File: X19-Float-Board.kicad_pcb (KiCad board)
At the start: 2 copper layers, 0 parts

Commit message: started layout
in meeting
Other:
- board outline added: 100 x 100 mm
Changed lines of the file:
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@@
 		)
+	)
+	(gr_circle
+		(center 150 100)
+		(end 200 100)
+		(stroke
+			(width 0.05)
+			(type solid)
+		)
+		(fill no)
+		(layer "Edge.Cuts")
 	)
 	(embedded_fonts no)

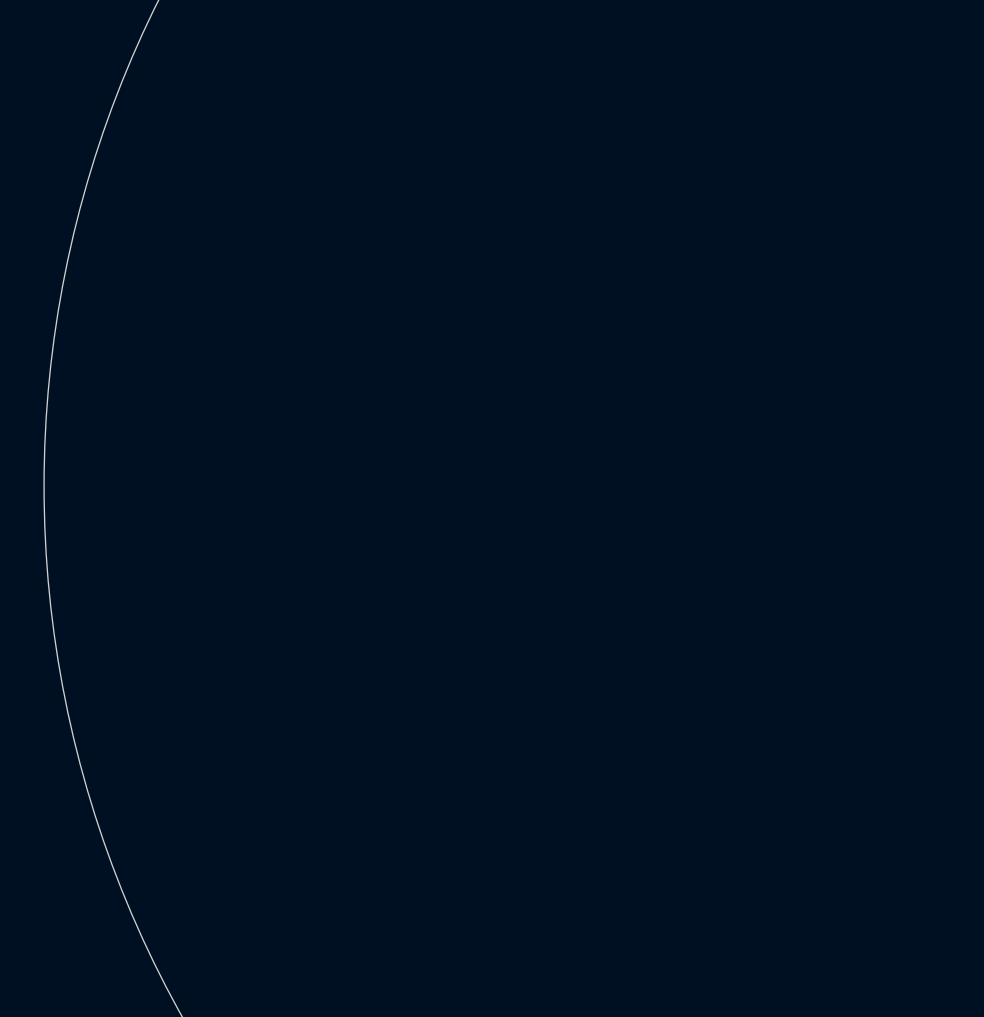
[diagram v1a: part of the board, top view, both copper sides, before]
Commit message: Footprint
Found footprints for multiple components and imported them to be used in PCB
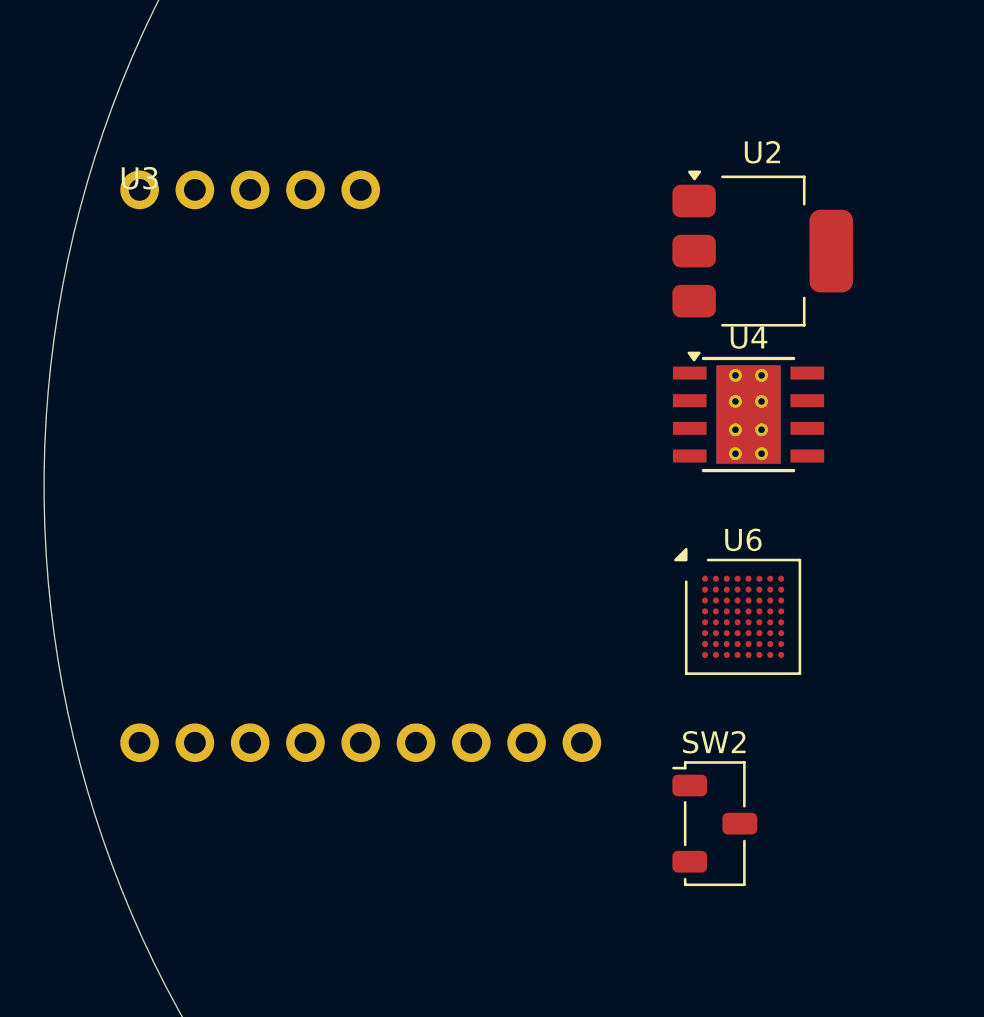
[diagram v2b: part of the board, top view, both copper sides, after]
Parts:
- added SW2: SW_Nidec_CAS-120A1, Button_Switch_SMD:Nidec_Copal_CAS-120A, F.Cu at (130.8, 115.5)
- added U2: AMS1117-3.3, Package_TO_SOT_SMD:SOT-223-3_TabPin2, F.Cu at (133.0, 89.2)
- added U3: RFM95W-868S2, customrf:rf module, F.Cu at (104.4, 86.4)
- added U4: TPS54336ADDA, Package_SO:TI_SO-PowerPAD-8_ThermalVias, F.Cu at (132.4, 96.7)
- added U6: STM32G431RBIx, Package_BGA:UFBGA-64_5x5mm_Layout8x8_P0.5mm, F.Cu at (132.1, 106.0)

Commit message: Custom RF module and component
Created my own setup for the footprint for the custom RF module
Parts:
- removed U3: RFM95W-868S2, customrf:rf module
- added C1: 100nF, Capacitor_SMD:C_0603_1608Metric, F.Cu at (169.6, 93.3)
- added C10: 100nF, Capacitor_SMD:C_0603_1608Metric, F.Cu at (162.0, 113.1)
- added C11: 100nF, Capacitor_SMD:C_0603_1608Metric, F.Cu at (163.6, 93.3)
- added C12: 100nF, Capacitor_SMD:C_0603_1608Metric, F.Cu at (169.6, 122.3)
- added C13: 100nF, Capacitor_SMD:C_0603_1608Metric, F.Cu at (175.6, 119.8)
- added C14: 4.7µF, Capacitor_SMD:C_0603_1608Metric, F.Cu at (169.6, 112.8)
- added C15: 4.7µF, Capacitor_SMD:C_0603_1608Metric, F.Cu at (169.6, 115.3)
- added C16: 4.7µF, Capacitor_SMD:C_0603_1608Metric, F.Cu at (169.6, 117.8)
- added C2: 27nF, Capacitor_SMD:C_0603_1608Metric, F.Cu at (169.6, 95.8)
- added C3: 10µF, Capacitor_SMD:C_0603_1608Metric, F.Cu at (169.6, 98.3)
- added C4: 120pF, Capacitor_SMD:C_0603_1608Metric, F.Cu at (169.6, 100.8)
- added C5: .012µF, Capacitor_SMD:C_0603_1608Metric, F.Cu at (169.6, 103.3)
- added C6: 0.1µF, Capacitor_SMD:C_0603_1608Metric, F.Cu at (173.6, 93.3)
- added C7: 47µF, Capacitor_SMD:C_0603_1608Metric, F.Cu at (173.6, 95.8)
- added C8: 47µF, Capacitor_SMD:C_0603_1608Metric, F.Cu at (173.6, 98.3)
- added C9: 100nF, Capacitor_SMD:C_0603_1608Metric, F.Cu at (175.6, 112.8)
- added D1: D_Schottky, Diode_SMD:D_SOD-123, F.Cu at (160.9, 105.0)
- added F1: 2A 12V PTC fuse, Fuse:Fuse_1812_4532Metric, F.Cu at (171.0, 107.0)
- added J1: Motor, TerminalBlock_Altech:Altech_AK100_1x02_P5.00mm, F.Cu at (153.0, 98.0)
- added J2: Conn_01x04_Pin, Connector_JST:JST_GH_BM04B-GHS-TBT_1x04-1MP_P1.25mm_Vertical, F.Cu at (154.8, 115.7)
- added L1: 15µH, Capacitor_SMD:C_0603_1608Metric, F.Cu at (173.6, 100.8)
- added Q1: NMOS, Package_SO:SO-8_3.9x4.9mm_P1.27mm, F.Cu at (153.7, 106.7)
- added R1: 220kΩ, Resistor_SMD:R_0603_1608Metric, F.Cu at (173.6, 103.3)
- added R11: 4.7kΩ, Resistor_SMD:R_0603_1608Metric, F.Cu at (162.0, 115.7)
- added R12: 4.7kΩ, Resistor_SMD:R_0603_1608Metric, F.Cu at (162.0, 118.2)
- added R13: 10kΩ, Resistor_SMD:R_0603_1608Metric, F.Cu at (163.6, 95.8)
- added R14: 220Ω, Resistor_SMD:R_0603_1608Metric, F.Cu at (163.6, 98.3)
- added R2: 43.2kΩ, Resistor_SMD:R_0603_1608Metric, F.Cu at (177.6, 93.3)
- added R3: 3.74kΩ, Resistor_SMD:R_0603_1608Metric, F.Cu at (177.6, 95.8)
- added R4: 100051Ω, Resistor_SMD:R_0603_1608Metric, F.Cu at (177.6, 98.3)
- added R5: 19.1kΩ, Resistor_SMD:R_0603_1608Metric, F.Cu at (177.6, 100.8)
- added R6: 10kΩ, Resistor_SMD:R_0603_1608Metric, F.Cu at (175.6, 115.3)
- added U1: ~, customrf:rf module, F.Cu at (108.4, 83.4)
- moved U4 47.0 mm to (176.7, 81.0)
- moved U2 33.0 mm to (165.2, 81.8)
- moved SW2 21.4 mm to (143.8, 98.5)
- moved U6 18.8 mm to (119.2, 92.2)

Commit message: Corrected stm32 symbol
made corrections to the stm32 for the package and the schmeatic
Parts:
- removed U6: STM32G431RBIx, Package_BGA:UFBGA-64_5x5mm_Layout8x8_P0.5mm
- added C13: 100nF, Capacitor_SMD:C_0603_1608Metric, F.Cu at (150.2, 126.0)
- added U3: STM32G431RBT6, stm32:LQFP64-10x10mm, F.Cu at (150.0, 58.5)
- moved U1 27.1 mm to (130.2, 99.4), turned to 180 degrees
- moved R12 6.44 mm to (156.5, 121.5)
- moved J2 5.09 mm to (150.5, 118.5)

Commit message: Modifications to power system to support what is required
modified
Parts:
- removed C1: 100nF, Capacitor_SMD:C_0603_1608Metric
- removed the C13 at (150.2, 126.0)
- removed the C13 at (175.6, 119.8)
- removed C15: 4.7µF, Capacitor_SMD:C_0603_1608Metric
- removed C2: 27nF, Capacitor_SMD:C_0603_1608Metric
- removed C3: 10µF, Capacitor_SMD:C_0603_1608Metric
- removed C4: 120pF, Capacitor_SMD:C_0603_1608Metric
- removed C5: .012µF, Capacitor_SMD:C_0603_1608Metric
- removed C6: 0.1µF, Capacitor_SMD:C_0603_1608Metric
- removed C7, C8: 47µF, Capacitor_SMD:C_0603_1608Metric
- removed L1: 15µH, Capacitor_SMD:C_0603_1608Metric
- removed R1: 220kΩ, Resistor_SMD:R_0603_1608Metric
- removed R2: 43.2kΩ, Resistor_SMD:R_0603_1608Metric
- removed R3: 3.74kΩ, Resistor_SMD:R_0603_1608Metric
- removed R4: 100051Ω, Resistor_SMD:R_0603_1608Metric
- removed R5: 19.1kΩ, Resistor_SMD:R_0603_1608Metric
- removed U4: TPS54336ADDA, Package_SO:TI_SO-PowerPAD-8_ThermalVias
- added C13: 100nF, Capacitor_SMD:C_0603_1608Metric, F.Cu at (234.6, 120.2)
- added D2: 1N5822, Diode_THT:D_DO-201AD_P15.24mm_Horizontal, F.Cu at (137.0, 134.2)
- added J3: Screw_Terminal_01x02, TerminalBlock_Altech:Altech_AK100_1x02_P5.00mm, F.Cu at (147.5, 130.9)
- U2: value AMS1117-3.3 -> LM2596S-3.3; footprint Package_TO_SOT_SMD:SOT-223-3_TabPin2 -> Package_TO_SOT_SMD:TO-263-5_TabPin3
- moved R12 107.2 mm to (258.8, 89.3)
- moved J2 105.9 mm to (251.5, 86.8)
- moved SW2 105.2 mm to (249.0, 96.1)
- moved C10 101.0 mm to (258.8, 84.3)
- moved R11 101.0 mm to (258.8, 86.8)
- moved C12 89.6 mm to (257.5, 105.4)
- moved C16 82.5 mm to (251.5, 107.9)
- moved C14 82.3 mm to (251.5, 105.4)
- moved C9 80.4 mm to (253.7, 93.9)
- moved R6 80.4 mm to (253.7, 96.4)
- moved Q1 66.1 mm to (218.7, 118.8)
- moved R13 66.1 mm to (228.6, 107.9)
- moved R14 66.1 mm to (228.6, 110.4)
- moved U2 39.6 mm to (150.0, 118.4), turned to -90 degrees
- moved U3 29.7 mm to (140.0, 86.5), turned to 180 degrees
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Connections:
- U2 pad 1: GND -> 12 V
- U2 pad 2: 3.3 V -> Net-(D2-K)
- U2 pad 3: 5 V -> GND
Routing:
- net GND: track 0.00 -> 38.4 mm
- net 12 V: track 0.00 -> 23.4 mm
- net 12V: track 0.00 -> 9.92 mm
- net Net-(D1-A): track 0.00 -> 9.23 mm
- net Net-(J3-Pin_2): track 0.00 -> 5.51 mm
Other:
- board size 100 x 100 mm -> 100.2 x 100.2 mm

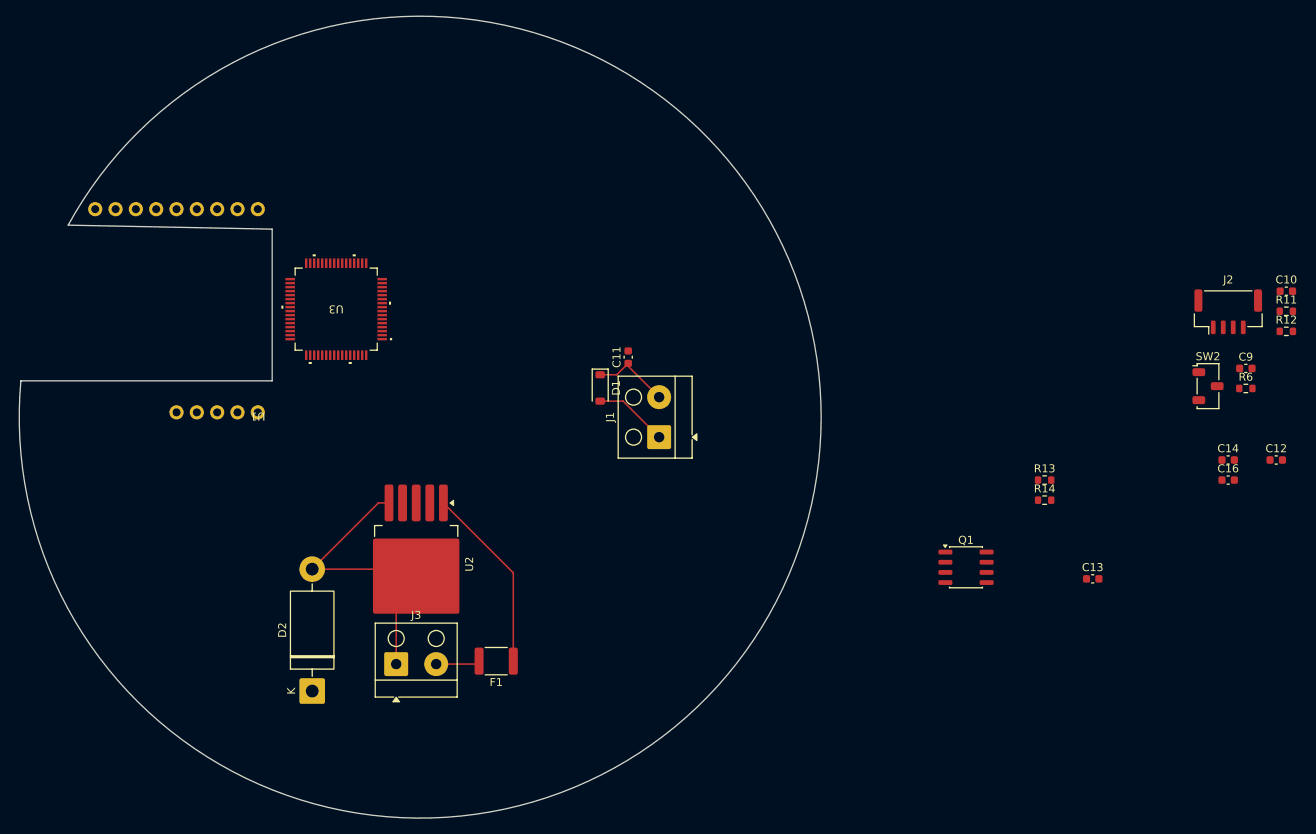
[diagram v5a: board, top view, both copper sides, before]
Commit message: Completed routing of PCB
Placed all components and routed pcb, large amount of drc errors, unsure
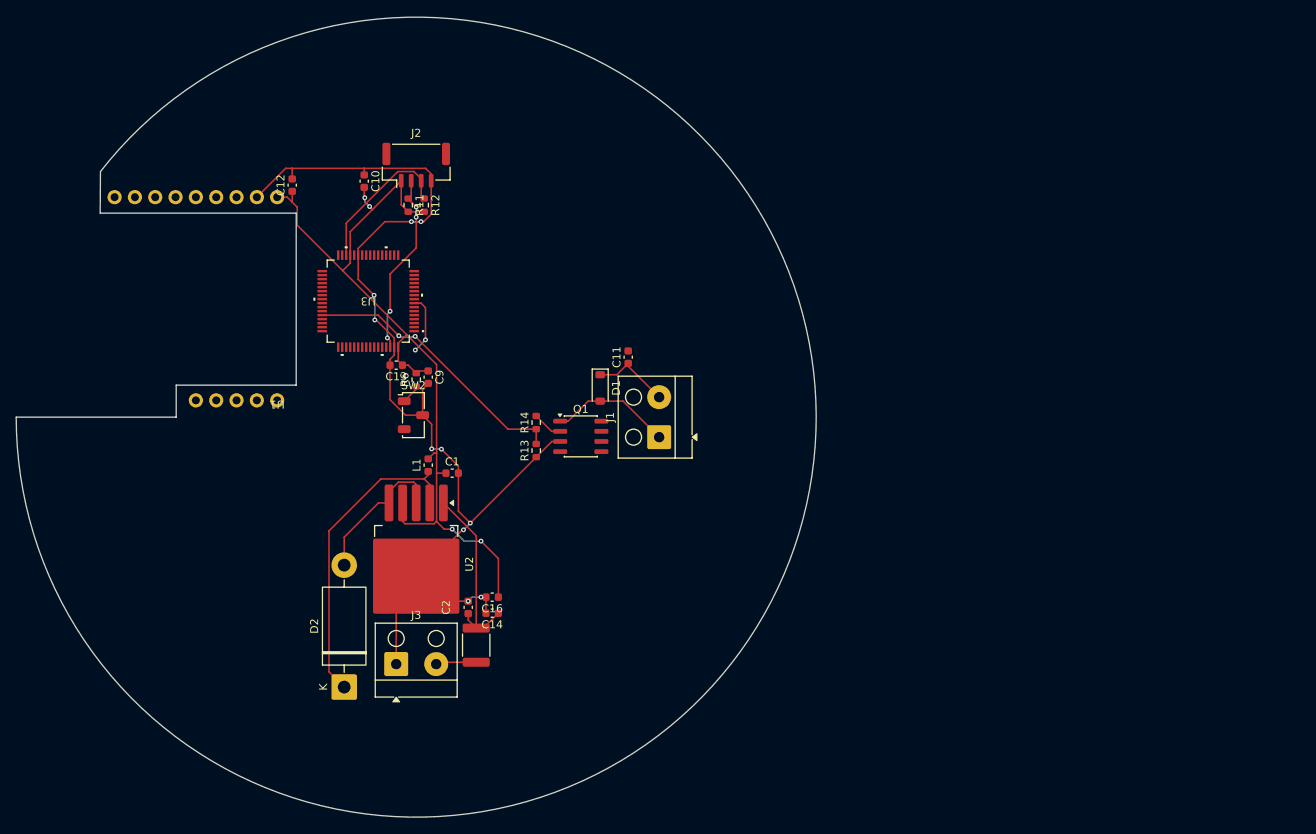
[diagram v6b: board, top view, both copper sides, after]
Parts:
- added C1: 220µF, Capacitor_SMD:C_0603_1608Metric, F.Cu at (154.5, 107.0)
- added C2: 680µF, Capacitor_SMD:C_0603_1608Metric, F.Cu at (156.5, 123.8)
- added L1: 33µH, Inductor_SMD:L_0603_1608Metric, F.Cu at (151.5, 106.0)
- moved C12 127.7 mm to (134.5, 71.0), turned to 90 degrees
- moved C10 116.1 mm to (143.5, 70.5), turned to -90 degrees
- moved R11 110.6 mm to (149.0, 73.5), turned to -90 degrees
- moved R12 108.9 mm to (151.0, 73.5), turned to -90 degrees
- moved R6 103.7 mm to (150.0, 95.3), turned to 90 degrees
- moved J2 103.1 mm to (150.0, 68.5)
- moved C9 102.2 mm to (151.5, 95.0), turned to -90 degrees
- moved SW2 99.4 mm to (149.7, 99.8)
- moved C14 94.0 mm to (159.5, 124.5), turned to 180 degrees
- moved C16 93.2 mm to (159.5, 122.5), turned to 180 degrees
- moved C13 91.1 mm to (147.5, 93.5), turned to 180 degrees
- moved R14 64.3 mm to (165.0, 100.7), turned to 90 degrees
- moved R13 63.7 mm to (165.0, 104.2), turned to 90 degrees
- moved Q1 50.9 mm to (170.6, 102.4)
- moved U3 4.12 mm to (144.0, 85.5)
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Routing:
- net GND: track 38.4 -> 162.5 mm, vias 0 -> 10
- net 3.3 V: track 0.00 -> 106.6 mm, vias 0 -> 4
- net Net-(D2-K): track 0.00 -> 39.3 mm
- net /Motor/Motor PWM: track 0.00 -> 34.6 mm, vias 0 -> 2
- net /sensor/Depth SCL: track 0.00 -> 23.0 mm, vias 0 -> 4
- net /sensor/Depth SDA: track 0.00 -> 19.0 mm
- net /Switch/switch: track 0.00 -> 9.94 mm, vias 0 -> 2
- net Net-(D1-A): track 9.23 -> 15.3 mm
- net Net-(Q1-G): track 0.00 -> 3.80 mm
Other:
- board size 100.2 x 100.2 mm -> 100 x 100 mm

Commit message: Finalized Traces
Potentially finallized traces
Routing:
- net /rf/RF MOSI: track 0.00 -> 47.7 mm, vias 0 -> 2
- net /rf/RF MISO: track 0.00 -> 40.6 mm, vias 0 -> 2
- net /rf/RF SCK: track 0.00 -> 39.4 mm, vias 0 -> 2
- net /rf/RF NSS: track 0.00 -> 36.4 mm, vias 0 -> 2
- net /rf/RF RST: track 0.00 -> 35.5 mm, vias 0 -> 4
- net /rf/RF INT: track 0.00 -> 33.9 mm, vias 0 -> 4
